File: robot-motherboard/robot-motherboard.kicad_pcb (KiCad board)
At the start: 2 copper layers, 30.5 x 53.3 mm, 1 part, among them U1 ESP32_PICO-1

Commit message: Finish layout
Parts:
- added C1: 100nF, Capacitor_THT:C_Disc_D3.0mm_W2.0mm_P2.50mm, F.Cu at (191.1, 79.4)
- added C10: 100nF, Capacitor_THT:C_Disc_D3.0mm_W2.0mm_P2.50mm, F.Cu at (134.0, 102.9)
- added C11: 100nF, Capacitor_THT:C_Disc_D3.0mm_W2.0mm_P2.50mm, F.Cu at (247.6, 103.5)
- added C12: 100nF, Capacitor_THT:C_Disc_D3.0mm_W2.0mm_P2.50mm, F.Cu at (226.6, 66.2)
- added C13: 100nF, Capacitor_THT:C_Disc_D3.0mm_W2.0mm_P2.50mm, F.Cu at (229.1, 44.3)
- added C2: 100nF, Capacitor_THT:C_Disc_D3.0mm_W2.0mm_P2.50mm, F.Cu at (257.8, 75.6)
- added C3: 100nF, Capacitor_THT:C_Disc_D3.0mm_W2.0mm_P2.50mm, F.Cu at (252.7, 103.5)
- added C4: 47uF, Capacitor_THT:CP_Radial_D5.0mm_P2.00mm, F.Cu at (206.3, 79.4)
- added C5: 47uF, Capacitor_THT:CP_Radial_D5.0mm_P2.00mm, F.Cu at (196.1, 79.4)
- added C6: 100nF, Capacitor_THT:C_Disc_D3.0mm_W2.0mm_P2.50mm, F.Cu at (257.8, 103.5)
- added C7: 100nF, Capacitor_THT:C_Disc_D3.0mm_W2.0mm_P2.50mm, F.Cu at (175.2, 94.0)
- added C8: 100nF, Capacitor_THT:C_Disc_D3.0mm_W2.0mm_P2.50mm, F.Cu at (258.6, 67.3)
- added C9: 100nF, Capacitor_THT:C_Disc_D3.0mm_W2.0mm_P2.50mm, F.Cu at (144.2, 61.6)
- added G1: SSD1306_OLED, GS_Development_Boards:ADAFRUIT_SSD1306_OLED, F.Cu at (154.9, 99.7)
- added H1: M3_PTH, MountingHole:MountingHole_3.2mm_M3_Pad, F.Cu at (145.4, 55.3)
- added H2: M3_PTH, MountingHole:MountingHole_3.2mm_M3_Pad, F.Cu at (135.2, 108.6)
- added H3: M3_PTH, MountingHole:MountingHole_3.2mm_M3_Pad, F.Cu at (255.2, 108.6)
- added H4: M3_PTH, MountingHole:MountingHole_3.2mm_M3_Pad, F.Cu at (227.8, 71.1)
- added H5: M3_PTH, MountingHole:MountingHole_3.2mm_M3_Pad, F.Cu at (227.8, 39.4)
- added J1: Wing0_S, GS_Connectors:JST_XH_S3B-XH-A-1_1x03_P2.50mm_Horizontal, F.Cu at (189.9, 42.6)
- added J10: Reflectance, Connector_JST:JST_XH_B4B-XH-A_1x04_P2.50mm_Vertical, F.Cu at (228.6, 51.6)
- added J11: Arm_I, Connector_JST:JST_XH_B3B-XH-A_1x03_P2.50mm_Vertical, F.Cu at (254.1, 44.4)
- added J12: Intake_I, Connector_JST:JST_XH_B3B-XH-A_1x03_P2.50mm_Vertical, F.Cu at (245.2, 44.4)
- added J13: User.Input, TerminalBlock:TerminalBlock_Xinya_XY308-2.54-4P_1x04_P2.54mm_Horizontal, F.Cu at (134.6, 90.8)
- added J14: I2C0, GS_Connectors:JST_XH_S4B-XH-A-1_1x04_P2.50mm_Horizontal, F.Cu at (220.3, 42.6)
- added J15: Extra, TerminalBlock:TerminalBlock_Xinya_XY308-2.54-5P_1x05_P2.54mm_Horizontal, F.Cu at (236.8, 110.2)
- added J16: I2C1, GS_Connectors:JST_XH_S4B-XH-A-1_1x04_P2.50mm_Horizontal, F.Cu at (205.1, 42.6)
- added J17: PW_OUT, TerminalBlock:TerminalBlock_Xinya_XY308-2.54-3P_1x03_P2.54mm_Horizontal, F.Cu at (134.6, 56.5)
- added J19: Basket_S, Connector_JST:JST_XH_B3B-XH-A_1x03_P2.50mm_Vertical, F.Cu at (236.3, 44.4)
- added J2: Wing0_SW, GS_Connectors:JST_XH_S3B-XH-A-1_1x03_P2.50mm_Horizontal, F.Cu at (177.2, 42.6)
- added J3: BATT, GS_Connectors:JST_XH_S2B-XH-A-1_1x02_P2.50mm_Horizontal, F.Cu at (140.9, 42.8)
- added J4: Wing1_S, GS_Connectors:JST_XH_S3B-XH-A-1_1x03_P2.50mm_Horizontal, F.Cu at (164.4, 42.6)
- added J5: Wing1_SW, GS_Connectors:JST_XH_S3B-XH-A-1_1x03_P2.50mm_Horizontal, F.Cu at (151.7, 42.6)
- added J6: 9V, TerminalBlock:TerminalBlock_Xinya_XY308-2.54-2P_1x02_P2.54mm_Horizontal, F.Cu at (134.6, 48.9)
- added J7: Drivetrain_M, Connector_JST:JST_XH_B5B-XH-A_1x05_P2.50mm_Vertical, F.Cu at (220.3, 108.7)
- added J8: Arm_M, Connector_JST:JST_XH_B5B-XH-A_1x05_P2.50mm_Vertical, F.Cu at (207.0, 85.9)
- added J9: Arm_M, Connector_JST:JST_XH_B5B-XH-A_1x05_P2.50mm_Vertical, F.Cu at (196.8, 85.9)
- added JP1: Battery bypass, Jumper:SolderJumper-2_P1.3mm_Open_TrianglePad1.0x1.5mm, B.Cu at (170.2, 59.6)
- added Q1: IRFZ44, Package_TO_SOT_THT:TO-220-3_Horizontal_TabDown, F.Cu at (165.1, 55.9)
- added R1: 470R, Resistor_THT:R_Axial_DIN0309_L9.0mm_D3.2mm_P12.70mm_Horizontal, F.Cu at (165.1, 50.2)
- added R2: 10K, Resistor_THT:R_Axial_DIN0309_L9.0mm_D3.2mm_P12.70mm_Horizontal, F.Cu at (168.9, 50.2)
- added R3: 4k7, Resistor_THT:R_Axial_DIN0309_L9.0mm_D3.2mm_P12.70mm_Horizontal, F.Cu at (207.6, 57.2)
- added R4: 4k7, Resistor_THT:R_Axial_DIN0309_L9.0mm_D3.2mm_P12.70mm_Horizontal, F.Cu at (207.6, 53.4)
- added R5: 4k7, Resistor_THT:R_Axial_DIN0309_L9.0mm_D3.2mm_P12.70mm_Horizontal, F.Cu at (191.8, 57.2)
- added R6: 4k7, Resistor_THT:R_Axial_DIN0309_L9.0mm_D3.2mm_P12.70mm_Horizontal, F.Cu at (191.8, 53.4)
- added RV1: POT1, GS_Resistors:ENPH253_Potentiometer, F.Cu at (176.5, 106.1)
- added RV2: POT2, GS_Resistors:ENPH253_Potentiometer, F.Cu at (187.9, 106.1)
- added RV3: POT3, GS_Resistors:ENPH253_Potentiometer, F.Cu at (199.4, 106.1)
- added RV4: POT4, GS_Resistors:ENPH253_Potentiometer, F.Cu at (210.8, 106.1)
- added S1: Logo, GS_Virtual:ENPH253_Logo, F.Cu at (186.0, 69.9)
- added U1: MCT6, Package_DIP:DIP-8_W7.62mm_LongPads, F.Cu at (152.9, 54.6)
- added U2: LM2596_Breakout, GS_Development_Boards:LM2596_Breakout, F.Cu at (155.1, 75.6)
- added U3: CD4051B, Package_DIP:DIP-16_W7.62mm_LongPads, F.Cu at (180.3, 79.4)
- added U5: BNO085, GS_Development_Boards:ADAFRUIT_BNO085, F.Cu at (245.6, 61.0)
- moved U4 88.9 mm to (236.2, 89.6), turned to 90 degrees
- renumbered U1 to U4
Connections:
- U4 pad 1: unconnected-(U1-TX0-Pad1) -> /TX0
- U4 pad 10: unconnected-(U1-GPIO10-Pad10) -> /ARM.INTAKE_PWM
- U4 pad 12: unconnected-(U1-GPIO12-Pad12) -> /GPIO12
- U4 pad 13: unconnected-(U1-GPIO13-Pad13) -> /DRIVETRAIN.M0_DIR
- U4 pad 14: unconnected-(U1-GPIO14-Pad14) -> /DRIVETRAIN.M1_PWM
- U4 pad 15: unconnected-(U1-GPIO15-Pad15) -> /BASKET.SERVO
- U4 pad 19: /M0.DIR -> /ARM.SHOULDER_PWM
- U4 pad 2: unconnected-(U1-GPIO2-Pad2) -> /GPIO2
- U4 pad 20: /M0.PWM -> /WING1.SERVO
- U4 pad 25: unconnected-(U1-GPIO25-Pad25) -> /INPUT.SELECT2
- U4 pad 26: unconnected-(U1-GPIO26-Pad26) -> /INPUT.MCU_IN
- U4 pad 27: unconnected-(U1-GPIO27-Pad27) -> /DRIVETRAIN.M1_DIR
- U4 pad 3: unconnected-(U1-RX0-Pad3) -> /RX0
- U4 pad 32: unconnected-(U1-GPIO32-Pad32) -> /WING0.LIMIT_SW_IN
- U4 pad 33: unconnected-(U1-GPIO33-Pad33) -> /WING1.LIMIT_SW_IN
- U4 pad 34: /M2.DIR -> /IR1.IN
- U4 pad 35: /M2.PWM -> /IR0.IN
- U4 pad 37: /M3.DIR -> /ARM.POSITION
- U4 pad 38: /M3.PWM -> /ARM.INTAKE_SW
- U4 pad 3V3: unconnected-(U1-Pad3V3) -> +3V3
- U4 pad 4: unconnected-(U1-GPIO4-Pad4) -> /DRIVETRAIN.M0_PWM
- U4 pad 5V: unconnected-(U1-Pad5V) -> +5V
- U4 pad 7: /M1.DIR -> /WING0.SERVO
- U4 pad 8: /M1.PWM -> /ARM.SHOULDER_DIR
- U4 pad 9: unconnected-(U1-GPIO9-Pad9) -> /ARM.INTAKE_DIR
- U4 pad VN: unconnected-(U1-GPIO39-PadVN) -> /INPUT.SELECT1
- U4 pad VP: unconnected-(U1-GPIO36-PadVP) -> /INPUT.SELECT0
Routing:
- net +3V3: track 0.00 -> 475.7 mm, vias 0 -> 1
- net +5V: track 0.00 -> 178.6 mm, vias 0 -> 5
- net /I2C0.SDA: track 0.00 -> 152.7 mm, vias 0 -> 1
- net /I2C0.SCL: track 0.00 -> 146.7 mm, vias 0 -> 1
- net /WING1.LIMIT_SW_IN: track 0.00 -> 133.7 mm, vias 0 -> 2
- net /WING0.LIMIT_SW_IN: track 0.00 -> 93.2 mm
- net /I2C1.SDA: track 0.00 -> 84.2 mm
- net /WING1.SERVO: track 0.00 -> 79.8 mm
- net +9V: track 0.00 -> 76.7 mm
- net /INPUT.MCU_IN: track 0.00 -> 70.6 mm
- net /I2C1.SCL: track 0.00 -> 67.7 mm, vias 0 -> 1
- net /WING0.SERVO: track 0.00 -> 64.5 mm
- net /BASKET.SERVO: track 0.00 -> 61.4 mm, vias 0 -> 1
- net Net-(J13-Pin_1): track 0.00 -> 52.1 mm
- net Net-(J13-Pin_2): track 0.00 -> 50.5 mm
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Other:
- board size 30.5 x 53.3 mm -> 129.3 x 78.7 mm
- board text added: "+"
- board text added: "-"
- board text added: "0"
- board text added: "0 mm"
- board text added: "0.01 mm"
- board text added: "0.02"
- board text added: "0.035 mm"
- board text added: "0.1000 mm / 0.1000 mm"
- board text added: "0.3000 mm"
- board text added: "0.D"
- board text added: "0.P"
- board text added: "1"
- board text added: "1.51 mm"
- board text added: "1.6000 mm"
- board text added: "1.D"
- board text added: "1.P"
- board text added: "12"
- board text added: "129.2860 mm x 78.7400 mm"
- board text added: "2"
- board text added: "3.3"
- board text added: "3V3"
- board text added: "4.5"
- board text added: "5V"
- board text added: "B.Cu"
- board text added: "B.Mask"
- board text added: "B.Paste"
- board text added: "B.Silkscreen"
- board text added: "BATT"
- board text added: "BOARD CHARACTERISTICS"
- board text added: "Board Thickness:"
- board text added: "Board overall dimensions:"
- board text added: "Bottom Silk Screen"
- board text added: "Bottom Solder Mask"
- board text added: "Bottom Solder Paste"
- board text added: "Castellated pads:"
- board text added: "Color"
- board text added: "Copper Finish:"
- board text added: "Copper Layer Count:"
- board text added: "Designed by George Sleen"
- board text added: "Dielectric"
- board text added: "Edge card connectors:"
- board text added: "Epsilon R"
- board text added: "F.Cu"
- board text added: "F.Mask"
- board text added: "F.Paste"
- board text added: "F.Silkscreen"
- board text added: "FR4"
- board text added: "GND"
- board text added: "I.D"
- board text added: "I.P"
- board text added: "IN"
- board text added: "IN0"
- board text added: "IN1"
- board text added: "IN5"
- board text added: "IN6"
- board text added: "IN7"
- board text added: "IN8"
- board text added: "Impedance Control:"
- board text added: "Layer Name"
- board text added: "Loss Tangent"
- board text added: "Material"
- board text added: "Min hole diameter:"
- board text added: "Min track/spacing:"
- board text added: "No"
- board text added: "None"
- board text added: "Not specified"
- board text added: "OUT"
- board text added: "PIN STRAPPING: GPIO0 -> PULL-UP GPIO2 -> PULL-DOWN MDTI(GPIO12) -> PULL-DOWN MDTO(GPIO15) -> PULL-UP GPIO5 -> PULL-UP"
- board text added: "Plated Board Edge:"
- board text added: "ROBOT MOTHERBOARD"
- board text added: "RX0"
- board text added: "S.D"
- board text added: "S.P"
- board text added: "SCL"
- board text added: "SDA"
- board text added: "TX0"
- board text added: "Thickness (mm)"
- board text added: "Top Silk Screen"
- board text added: "Top Solder Mask"
- board text added: "Top Solder Paste"
- board text added: "Type"
- board text added: "copper"
- board text added: "core"
- board text added: "github.com /enph253-2025-team5/ robot-motherboard-pcb"

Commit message: Generate production files
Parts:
- added REF**: OSHW-Logo_11.4x12mm_SilkScreen, Symbol:OSHW-Logo_11.4x12mm_SilkScreen, B.Cu at (165.1, 76.2)

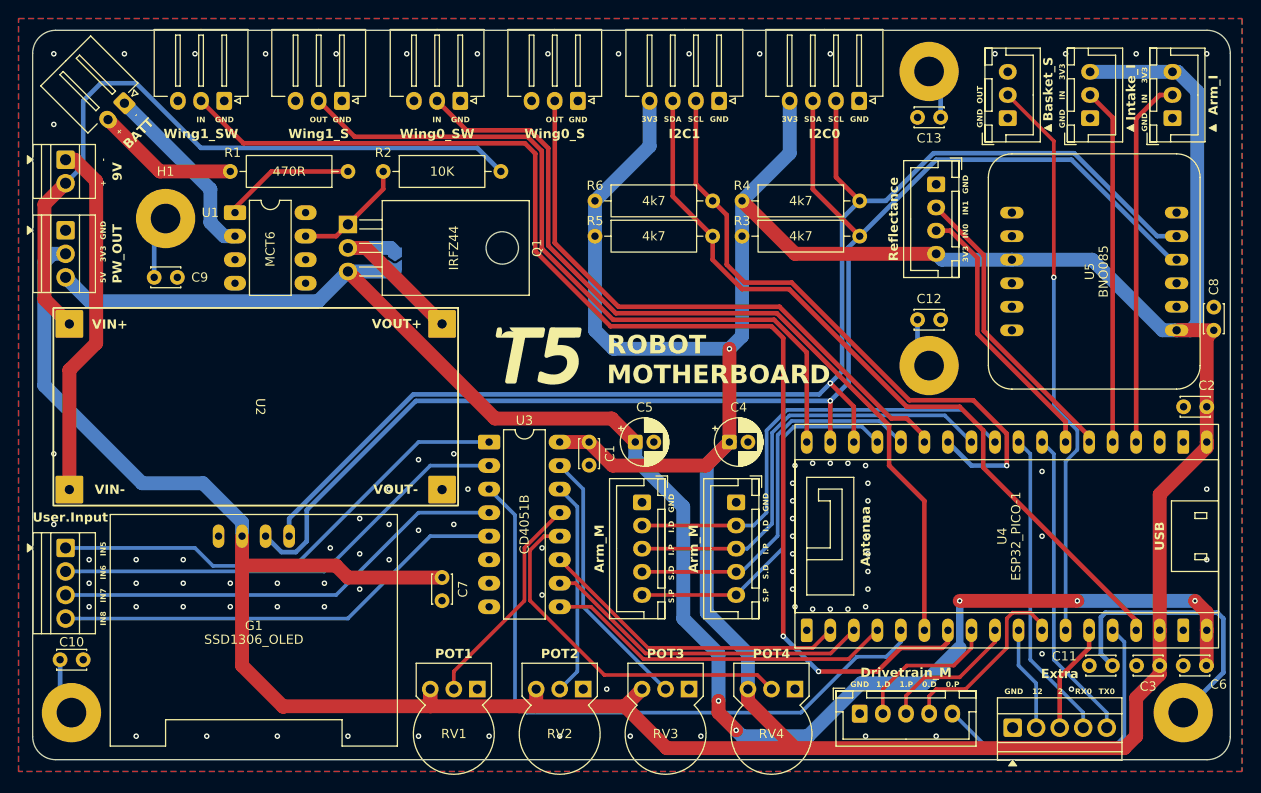
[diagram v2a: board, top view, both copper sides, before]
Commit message: Add filtering on user input
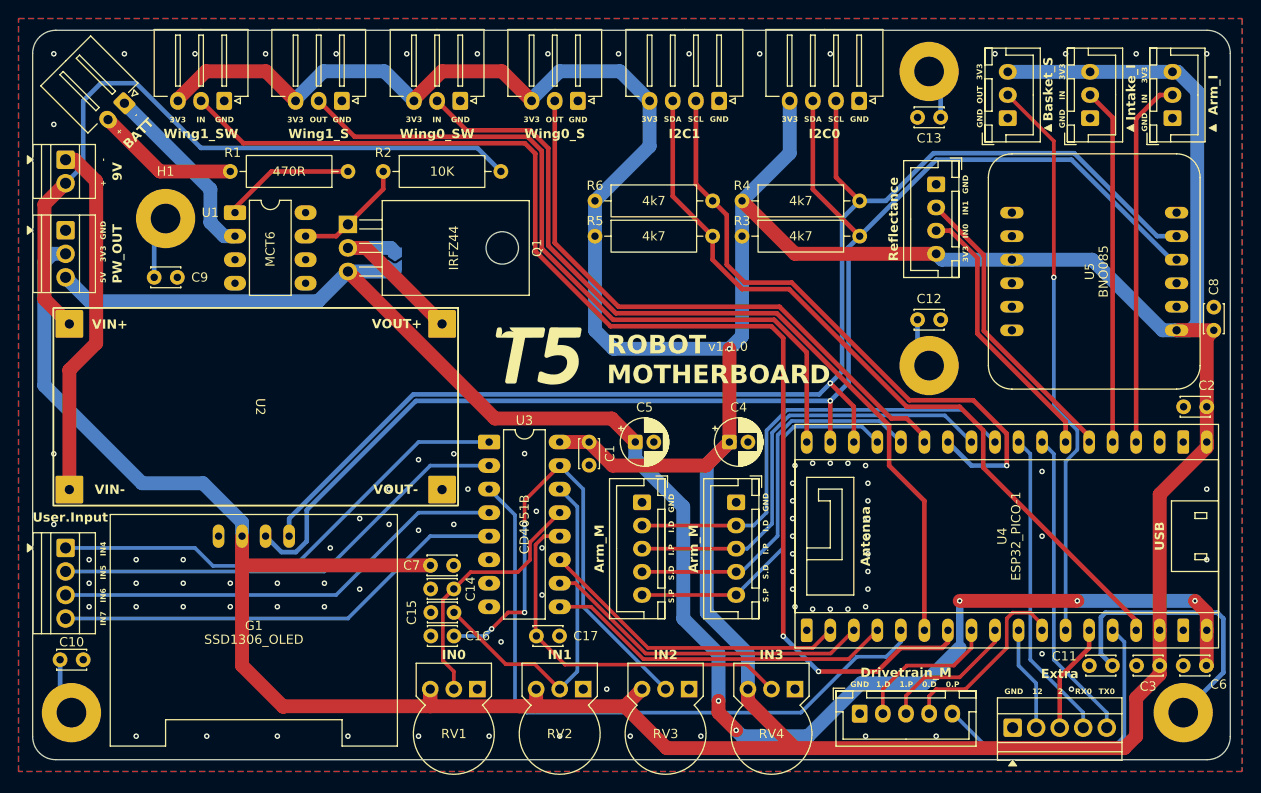
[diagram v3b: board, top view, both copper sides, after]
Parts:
- removed REF**: OSHW-Logo_11.4x12mm_SilkScreen, Symbol:OSHW-Logo_11.4x12mm_SilkScreen
- added C14: 100nF, Capacitor_THT:C_Disc_D3.0mm_W2.0mm_P2.50mm, F.Cu at (176.5, 95.2)
- added C15: 100nF, Capacitor_THT:C_Disc_D3.0mm_W2.0mm_P2.50mm, F.Cu at (176.5, 97.8)
- added C16: 100nF, Capacitor_THT:C_Disc_D3.0mm_W2.0mm_P2.50mm, F.Cu at (176.5, 100.3)
- added C17: 100nF, Capacitor_THT:C_Disc_D3.0mm_W2.0mm_P2.50mm, F.Cu at (185.4, 100.3)
- RV1: value POT1 -> IN0
- RV2: value POT2 -> IN1
- RV3: value POT3 -> IN2
- RV4: value POT4 -> IN3
- moved C7 1.81 mm to (174.0, 92.7), turned to 0 degrees
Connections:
- J1 pad 3: unconnected-(J1-Pin_3-Pad3) -> +3V3
- J19 pad 3: unconnected-(J19-Pin_3-Pad3) -> +3V3
- J2 pad 3: unconnected-(J2-Pin_3-Pad3) -> +3V3
- J4 pad 3: unconnected-(J4-Pin_3-Pad3) -> +3V3
- J5 pad 3: unconnected-(J5-Pin_3-Pad3) -> +3V3
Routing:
- net +3V3: track 475.7 -> 544.7 mm
- net Net-(U3-X2): track 28.9 -> 55.0 mm, vias 0 -> 3
- net Net-(U3-X1): track 23.2 -> 38.0 mm
- net Net-(U3-X0): track 23.8 -> 27.8 mm
- net Net-(U3-X3): track 39.3 -> 40.6 mm
- net GND: vias 90 -> 91
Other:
- board text added: "${REVISION}"
- board text added: "IN4"
- board text removed: "IN8"

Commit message: Update back silkscreen
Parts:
- added REF**: OSHW-Logo_11.4x12mm_SilkScreen, Symbol:OSHW-Logo_11.4x12mm_SilkScreen, B.Cu at (166.4, 76.2)
- added REF**: KiCad-Logo2_12mm_SilkScreen, Symbol:KiCad-Logo2_12mm_SilkScreen, B.Cu at (196.8, 66.0)

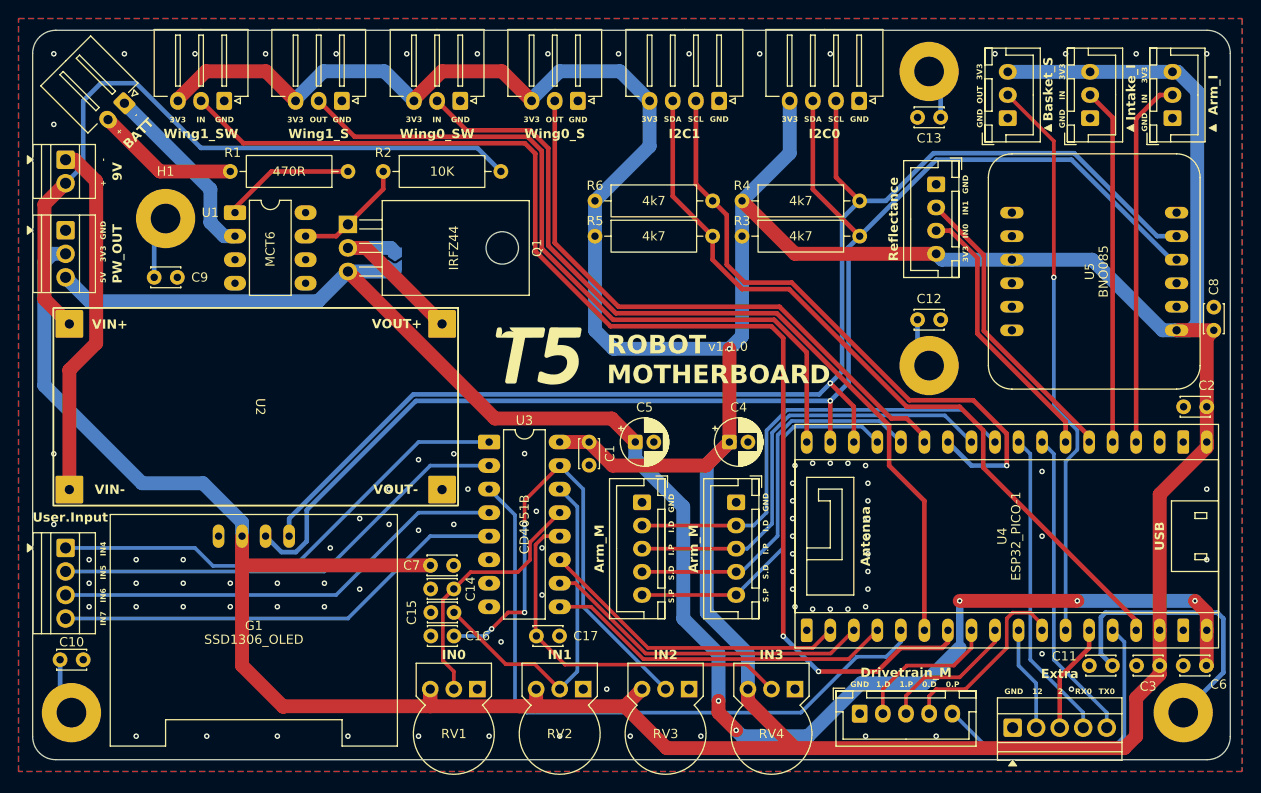
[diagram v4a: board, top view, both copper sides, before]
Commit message: Update board outline for better access to power jumper
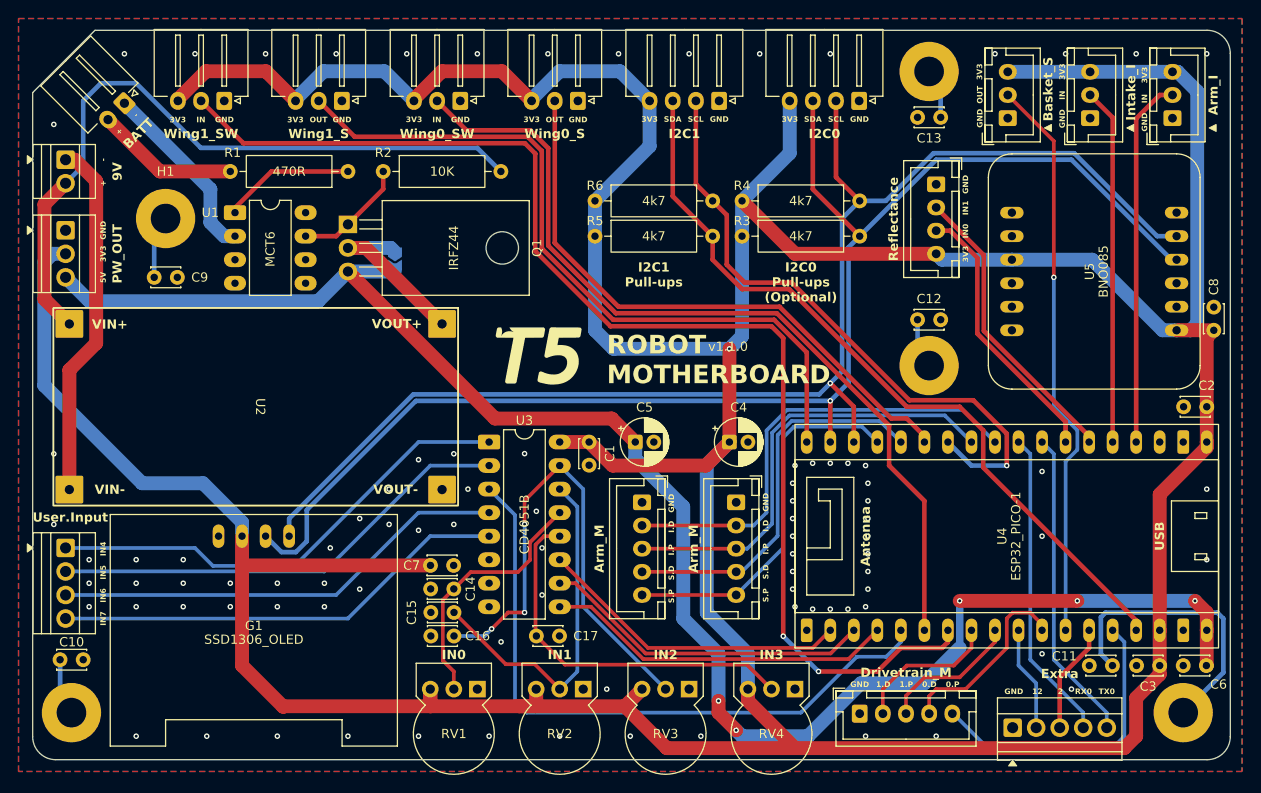
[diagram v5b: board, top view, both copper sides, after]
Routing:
- net GND: vias 91 -> 90
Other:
- outline, holes or cut-outs redrawn
- board text added: "I2C0 Pull-ups (Optional)"
- board text added: "I2C1 Pull-ups"
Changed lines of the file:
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@@
 	(gr_line
 		(start 131.044 111.185)
-		(end 131.044 37.445)
+		(end 131.044 41.6814)
+		(stroke
+			(width 0.05)
+			(type default)
+		)
+		(layer "Edge.Cuts")
+	)
+	(gr_line
+		(start 131.044 41.676)
+		(end 137.775 34.945)
 		(stroke
 			(width 0.05)
@@
 	)
 	(gr_line
-		(start 133.544 34.945)
+		(start 137.775 34.945)
 		(end 257.83 34.945)
 		(stroke
@@
 	)
 	(gr_arc
-		(start 131.044 37.445)
-		(mid 131.776233 35.677233)
-		(end 133.544 34.945)
-		(stroke
-			(width 0.05)
-			(type default)
-		)
-		(layer "Edge.Cuts")
-	)
-	(gr_arc
 		(start 133.544 113.685)
 		(mid 131.776233 112.952767)
@@
 		)
 	)
+	(gr_text "I2C0\nPull-ups\n(Optional)"
+		(at 213.975 59.944 0)
+		(layer "F.SilkS")
+		(effects
+			(font
+				(size 1 1)
+				(thickness 0.2)
+				(bold yes)
+			)
+			(justify top)
+		)
+	)
 	(gr_text "S.D"
 		(at 210.1904 93.4158 90)
@@
 		)
 	)
+	(gr_text "I2C1\nPull-ups"
+		(at 198.1 59.944 0)
+		(layer "F.SilkS")
+		(effects
+			(font
+				(size 1 1)
+				(thickness 0.2)
+				(bold yes)
+			)
+			(justify top)
+		)
+	)
 	(gr_text "IN"
 		(at 174.6812 44.597 0)
@@
 		(size 0.6)
 		(drill 0.3)
-		(layers "F.Cu" "B.Cu")
-		(free yes)
-		(net 1)
-	)
-	(via
-		(at 133.33 37.485)
-		(size 0.6)
-		(drill 0.3)

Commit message: Add switches between user input and encoder inputs
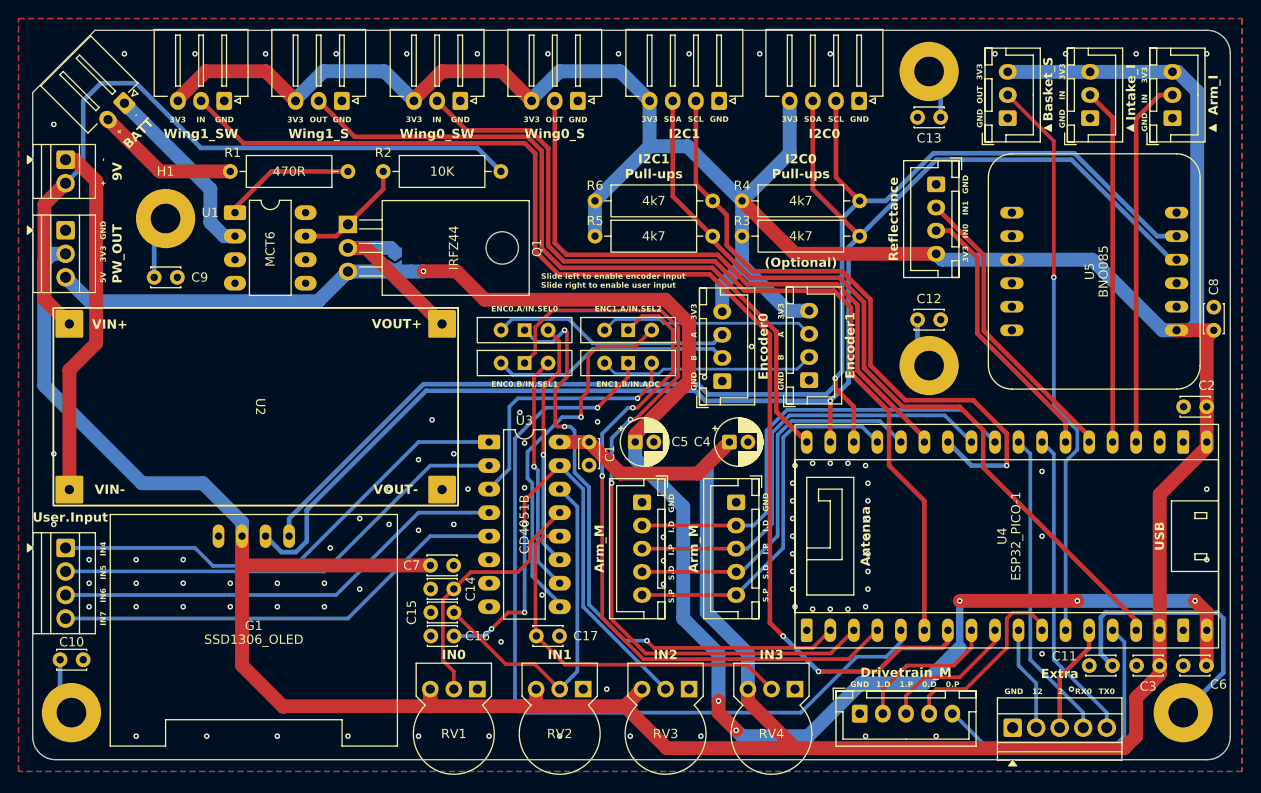
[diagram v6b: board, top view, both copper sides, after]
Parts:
- removed the REF** at (196.8, 66.0)
- added J18: Encoder1, Connector_JST:JST_XH_B4B-XH-A_1x04_P2.50mm_Vertical, F.Cu at (214.9, 72.7)
- added J20: Encoder0, Connector_JST:JST_XH_B4B-XH-A_1x04_P2.50mm_Vertical, F.Cu at (205.5, 72.8)
- added REF**: KiCad-Logo2_8mm_SilkScreen, Symbol:KiCad-Logo2_8mm_SilkScreen, B.Cu at (205.7, 54.5)
- added SW1: ENC0.A/IN.SEL0, Button_Switch_THT:SW_Slide-03_Wuerth-WS-SLTV_10x2.5x6.4_P2.54mm, F.Cu at (184.2, 67.3)
- added SW2: ENC0.B/IN.SEL1, Button_Switch_THT:SW_Slide-03_Wuerth-WS-SLTV_10x2.5x6.4_P2.54mm, F.Cu at (184.2, 70.9)
- added SW3: ENC1.A/IN.SEL2, Button_Switch_THT:SW_Slide-03_Wuerth-WS-SLTV_10x2.5x6.4_P2.54mm, F.Cu at (195.3, 67.3)
- added SW4: ENC1.B/IN.ADC, Button_Switch_THT:SW_Slide-03_Wuerth-WS-SLTV_10x2.5x6.4_P2.54mm, F.Cu at (195.3, 70.9)
- S1: moved to B.Cu
- moved S1 68.7 mm to (252.0, 89.2), turned to 180 degrees
- moved REF** 1.37 mm to (165.1, 75.7)
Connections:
- U3 pad 3: /INPUT.MCU_IN -> /INPUT.ADC_IN
- U4 pad 25: /INPUT.SELECT2 -> /SWITCH3
- U4 pad 26: /INPUT.MCU_IN -> /SWITCH4
- U4 pad VN: /INPUT.SELECT1 -> /SWITCH2
- U4 pad VP: /INPUT.SELECT0 -> /SWITCH1
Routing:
- net /SWITCH4: track 0.00 -> 91.4 mm, vias 0 -> 1
- net /SWITCH2: track 0.00 -> 84.8 mm, vias 0 -> 2
- net /SWITCH3: track 0.00 -> 73.7 mm, vias 0 -> 2
- net /INPUT.MCU_IN: track 70.6 -> 0.00 mm
- net /SWITCH1: track 0.00 -> 66.7 mm, vias 0 -> 3
- net /INPUT.ADC_IN: track 0.00 -> 28.5 mm, vias 0 -> 1
- net /ENCODER0.B: track 0.00 -> 26.0 mm
- net /ENCODER0.A: track 0.00 -> 25.8 mm
- net /ENCODER1.B: track 0.00 -> 23.3 mm
- net /ENCODER1.A: track 0.00 -> 23.2 mm
- net +3V3: track 544.7 -> 527.9 mm, vias 1 -> 0
- net +5V: track 178.6 -> 189.4 mm, vias 5 -> 6
- net /INPUT.SELECT1: track 35.9 -> 25.5 mm, vias 0 -> 1
- net /INPUT.SELECT0: track 33.9 -> 26.7 mm, vias 0 -> 1
- net /WING0.LIMIT_SW_IN: track 93.2 -> 98.2 mm
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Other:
- board text added: "(Optional)"
- board text added: "20 = Wing1.Servo 21 = I2C0.SDA 22 = I2C0.SCL 19 = Arm.Shoulder_PWM 08 = Arm.Shoulder_Dir 07 = Wing0.Servo 05 = I2C1.SCL 10 = Arm.Intake_PWM 09 = Arm.Intake_Dir 03 = RX0* 01 = TX0* 35 = IR0 34 = IR1 38 = Arm.Intake_Sw 37 = Arm.Position"
- board text added: "A"
- board text added: "B"
- board text added: "I2C0 Pull-ups"
- board text added: "Pin strapping: 00 -> Pull-up 02 -> Pull-down 12 -> Pull-down 15 -> Pull-up 05 -> Pull-up"
- board text added: "Slide left to enable encoder input Slide right to enable user input"
- board text added: "VP = Encoder0.A VN = Encoder0.B 25 = Encoder1.A 26 = Encoder1.B 32 = Wing0.SW 33 = Wing1.SW 27 = Drive.M1_Dir 14 = Drive.M1_PWM 12 = free* 13 = Drive.M0_Dir 15 = Basket.Servo 02 = free* 04 = Drive.M0_PWM 00 = I2C1.SDA"
- board text removed: "I2C0 Pull-ups (Optional)"
- board text removed: "PIN STRAPPING: GPIO0 -> PULL-UP GPIO2 -> PULL-DOWN MDTI(GPIO12) -> PULL-DOWN MDTO(GPIO15) -> PULL-UP GPIO5 -> PULL-UP"
